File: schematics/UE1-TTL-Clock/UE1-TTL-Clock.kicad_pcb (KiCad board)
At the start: 2 copper layers, 76.8 x 99.1 mm, 79 parts, among them J1 Edge 1, J2 Edge 2, SW1 RUN, SW2 HALT, SW3 RESET, U1 74LS74, U2 74LS08, U3 NE555, U4 NE555, U5 74LS132, U6 74LS02

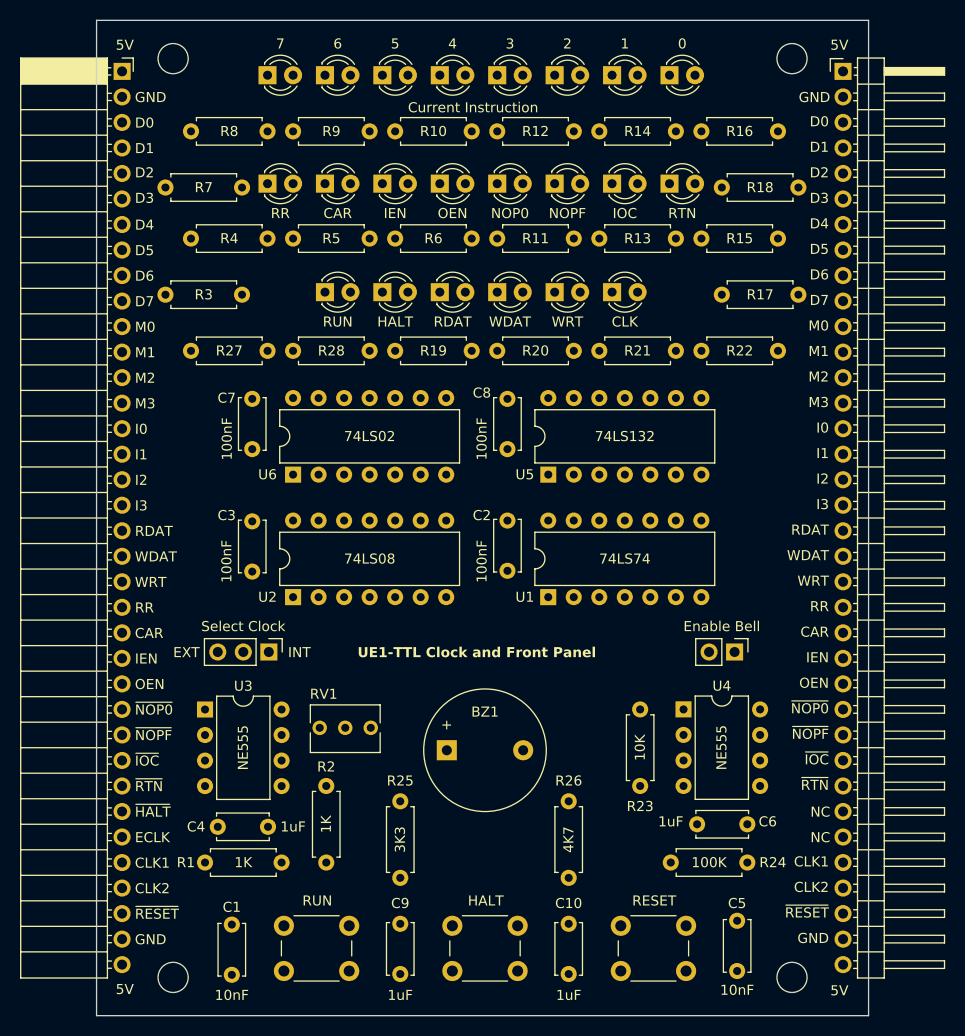
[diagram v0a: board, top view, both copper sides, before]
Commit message: Lay out clock board
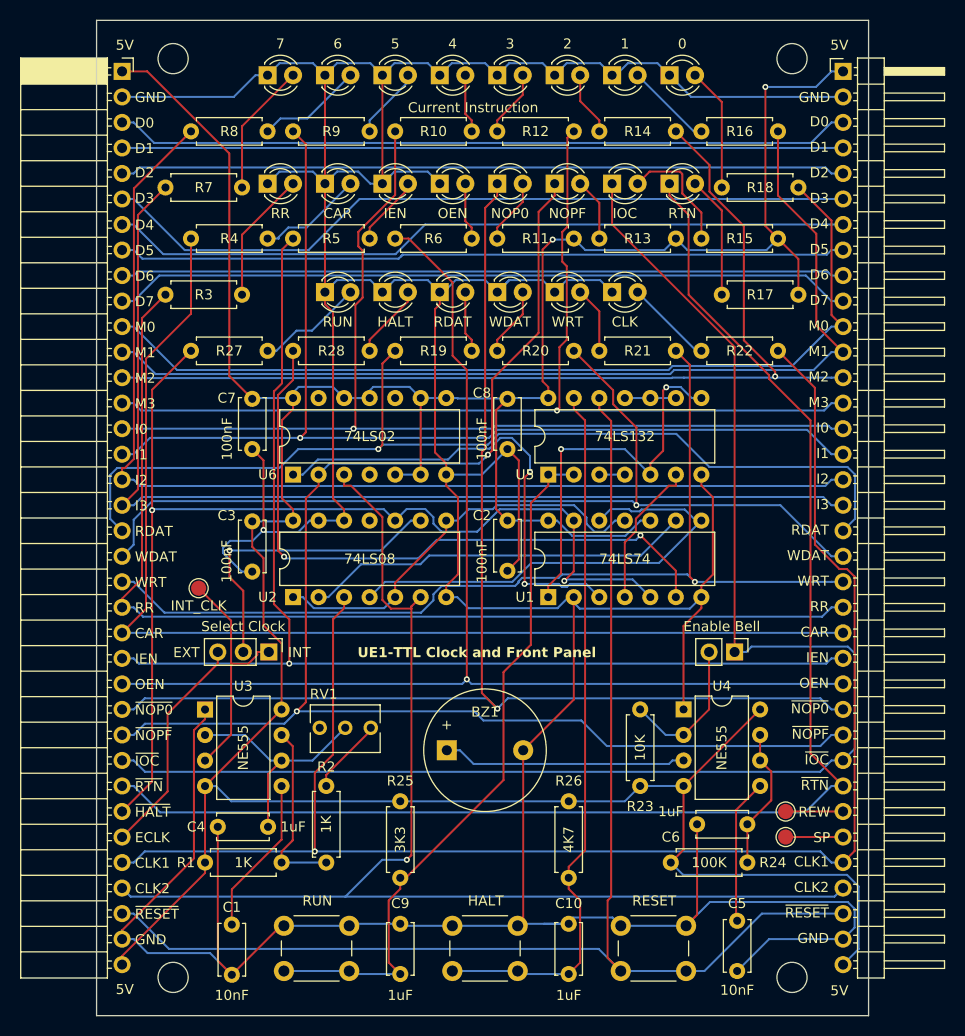
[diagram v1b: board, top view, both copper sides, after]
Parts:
- added TP1: REWIND, TestPoint:TestPoint_Pad_D1.5mm, F.Cu at (156.2, 127.0)
- added TP2: SPARE, TestPoint:TestPoint_Pad_D1.5mm, F.Cu at (156.2, 129.5)
- added TP3: INT_CLK, TestPoint:TestPoint_Pad_D1.5mm, F.Cu at (97.8, 104.8)
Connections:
- J2 pad 30: unconnected-(J2-Pin_30-Pad30) -> Net-(J2-Pin_30)
- J2 pad 31: unconnected-(J2-Pin_31-Pad31) -> Net-(J2-Pin_31)
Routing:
- net GND: track 0.00 -> 506.9 mm, vias 0 -> 1
- net +5V: track 0.00 -> 348.1 mm, vias 0 -> 2
- net CLK1: track 0.00 -> 154.2 mm, vias 0 -> 1
- net ~{OP_IOC}: track 0.00 -> 148.0 mm
- net ~{OP_NOPF}: track 0.00 -> 146.5 mm, vias 0 -> 2
- net ~{OP_RTN}: track 0.00 -> 141.0 mm
- net ~{RESET}: track 0.00 -> 134.7 mm
- net ~{OP_NOP0}: track 0.00 -> 127.1 mm, vias 0 -> 1
- net CLK2: track 0.00 -> 124.5 mm, vias 0 -> 1
- net OEN: track 0.00 -> 119.7 mm, vias 0 -> 1
- net IEN: track 0.00 -> 115.9 mm, vias 0 -> 1
- net CAR: track 0.00 -> 113.8 mm
- net ~{HALTED}: track 0.00 -> 110.3 mm, vias 0 -> 2
- net INST2: track 0.00 -> 109.9 mm
- net INST3: track 0.00 -> 105.8 mm
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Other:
- board text added: "REW"
- board text added: "SP"
- board text removed: "NC"
